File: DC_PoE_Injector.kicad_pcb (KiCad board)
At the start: 4 copper layers, 67.3 x 102.7 mm, 71 parts, among them J1 PWR IN, J2 R-RJ45R08P-C000, J3 R-RJ45R08P-C000, J4 54V Test Points, Q1 IRLR3410TRPBF, Q2 CSD19537Q3T, T1 SM51625EL, U1 TPS23861, U2 LM5155QDSSRQ1, U3 TPS7B8233QDGNRQ1

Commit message: Some cleanups
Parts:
- Q1: footprint Package_TO_SOT_SMD:TO-252-2 -> CakeKiCadLib:TO-252-2-JLCPCB
- U2: footprint CakeKiCadLib:LM5155QDSSRQ1 -> CakeKiCadLib:DSS0012x
- U3: footprint CakeKiCadLib:TPS7B8233QDGNRQ1 -> CakeKiCadLib:DGN0008G
- moved F1 1.10 mm to (83.9, 117.4)
- moved Q1 0.89 mm to (82.5, 128.4), turned to 180 degrees
- moved C7 0.80 mm to (77.2, 104.0)
- moved R8 0.80 mm to (77.2, 100.5)
- moved Q2 0.50 mm to (88.2, 84.2)
- moved R16 0.30 mm to (94.8, 85.2)
- turned C14 to 90 degrees
- turned C20 to 180 degrees
- turned C21 to 180 degrees
- turned U2 to -90 degrees
- turned U3 to 180 degrees
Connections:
- Q2 pad 1: Net-(D3-A) -> Net-(Q2-S)
- Q2 pad 3: Net-(Q2-S) -> Net-(D3-A)
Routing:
- net GND: track 53.8 -> 69.3 mm, vias 78 -> 111
- net POE_78: track 24.1 -> 18.3 mm, vias 12 -> 13
- net Net-(C12-Pad1): track 4.00 -> 2.00 mm
- net Net-(Q2-S): track 11.9 -> 10.6 mm
- net POE_12: track 27.6 -> 27.1 mm
- added copper zone on In1.Cu, net VCC
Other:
- board size 67.3 x 102.7 mm -> 68.1 x 102.5 mm

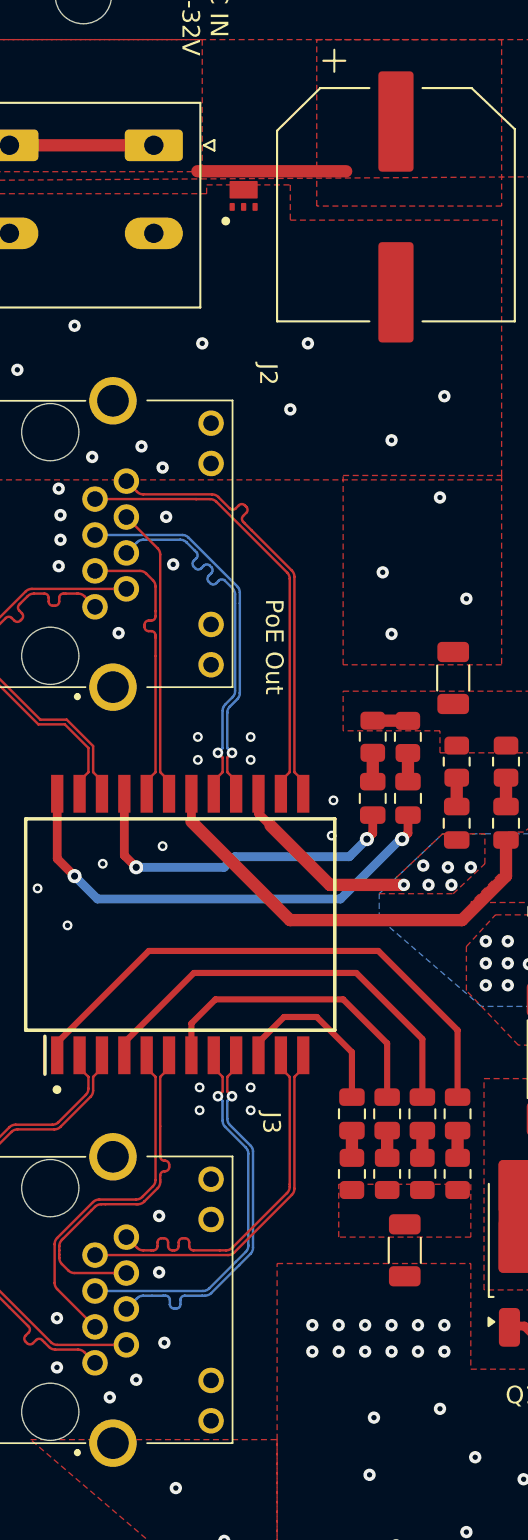
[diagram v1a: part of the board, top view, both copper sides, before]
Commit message: add silkscreen labels for power
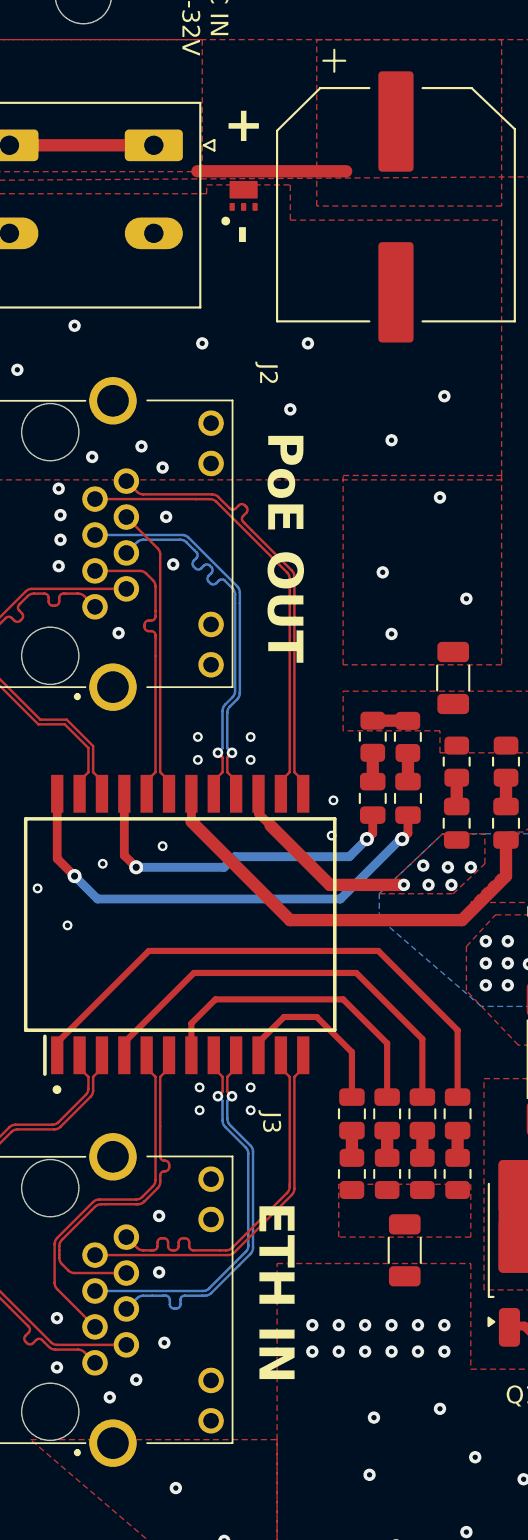
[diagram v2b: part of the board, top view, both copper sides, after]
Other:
- board text added: "+"
- board text added: "-"
- board text added: "ETH IN"
- board text added: "PoE OUT"
- board text removed: "PoE Out"
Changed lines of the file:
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@@
 		)
 	)
-	(gr_text "PoE Out"
-		(at 66.25 91.25 270)
+	(gr_text "PoE OUT"
+		(at 66.25 81.75 270)
 		(layer "F.SilkS")
 		(effects
 			(font
-				(size 1 1)
-				(thickness 0.153)
+				(size 2 2)
+				(thickness 0.4)
+				(bold yes)
+			)
+			(justify left bottom)
+		)
+	)
+	(gr_text "ETH IN"
+		(at 65.75 125.5 270)
+		(layer "F.SilkS")
+		(effects
+			(font
+				(size 2 2)
+				(thickness 0.4)
+				(bold yes)
+			)
+			(justify left bottom)
+		)
+	)
+	(gr_text "-"
+		(at 64 70 270)
+		(layer "F.SilkS")
+		(effects
+			(font
+				(size 2 2)
+				(thickness 0.5)
+				(bold yes)
+			)
+			(justify left bottom)
+		)
+	)
+	(gr_text "+"
+		(at 64 63.25 270)
+		(layer "F.SilkS")
+		(effects
+			(font
+				(size 2 2)
+				(thickness 0.5)
+				(bold yes)
 			)
 			(justify left bottom)
@@
 			(pts
 				(xy 78.8 104.6) (xy 84.2 104.6) (xy 84.2 114.4) (xy 78.6 114.4) (xy 72.8 109.4) (xy 72.8 108) (xy 76.4 104.6)
-				(xy 78.8 104.6)
 			)
 		)
